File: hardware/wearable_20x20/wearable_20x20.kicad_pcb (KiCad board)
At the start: 4 copper layers, 49.3 x 49.3 mm, 400 parts

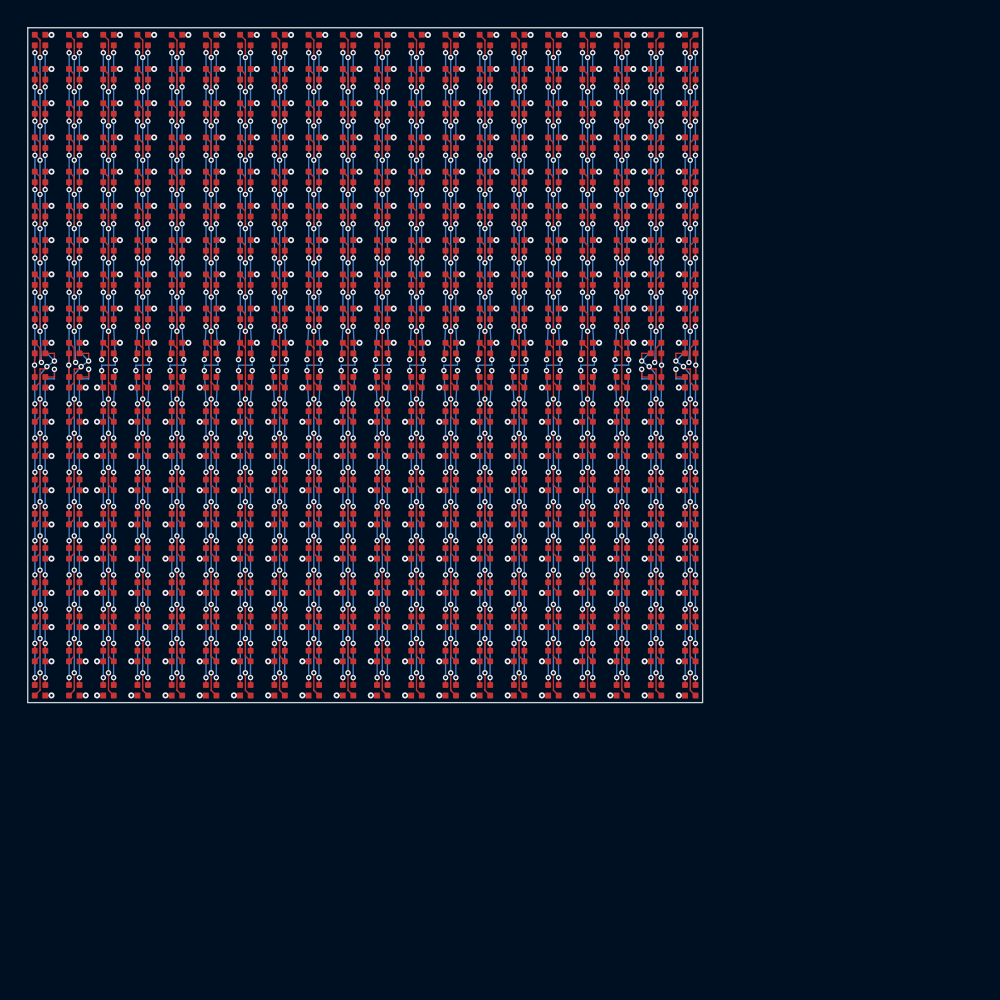
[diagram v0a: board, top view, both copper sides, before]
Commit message: Place 20x20 backside parts outside the via field
Co-authored-by: illiapliukhin <illiapliukhin@users.noreply.github.com>
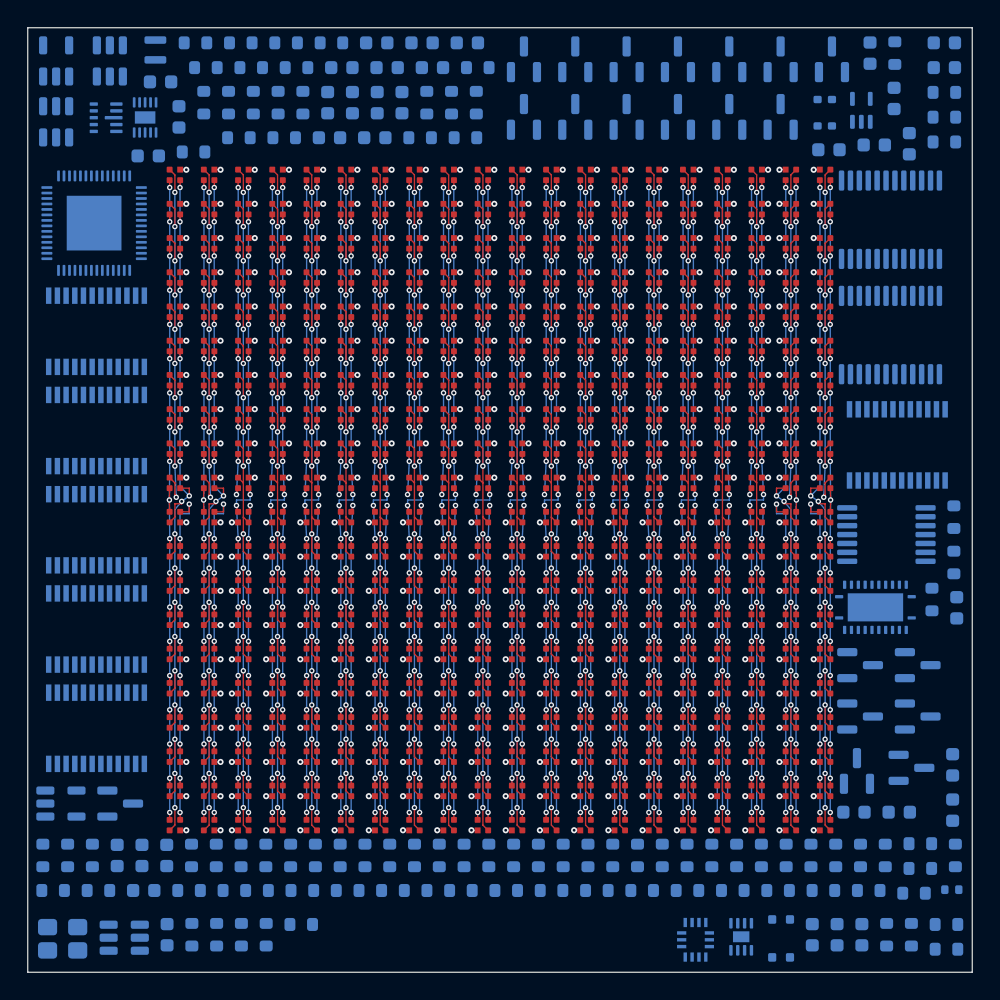
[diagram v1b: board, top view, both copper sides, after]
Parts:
- added C1: 1uF, C_0603_1608Metric, B.Cu at (22.0, 8.03)
- added C10: 10uF, C_0603_1608Metric, B.Cu at (25.5, 5.47)
- added C100: 100nF, C_0603_1608Metric, B.Cu at (67.9, 42.4)
- added C101: 100nF, C_0603_1608Metric, B.Cu at (67.6, 53.8)
- added C102: 100nF, C_0603_1608Metric, B.Cu at (67.6, 57.2)
- added C103: 100nF, C_0603_1608Metric, B.Cu at (60.4, 57.3)
- added C104: 100nF, C_0603_1608Metric, B.Cu at (63.7, 57.3)
- added C105: 100nF, C_0603_1608Metric, B.Cu at (8.80, 9.37)
- added C106: 100nF, C_0603_1608Metric, B.Cu at (9.71, 3.95)
- added C107: 100nF, C_0603_1608Metric, B.Cu at (11.1, 6.51)
- added C11: 1nF, C_0603_1608Metric, B.Cu at (27.3, 5.47)
- added C12: 10uF, C_0603_1608Metric, B.Cu at (29.6, 2.91)
- added C2: 10uF, C_0603_1608Metric, B.Cu at (21.9, 5.47)
- added C20: 1uF, C_0603_1608Metric, B.Cu at (10.2, 66.3)
- added C201: 100nF, C_0603_1608Metric, B.Cu at (6.53, 60.5)
- added C202: 100nF, C_0603_1608Metric, B.Cu at (8.47, 63.0)
- added C203: 100nF, C_0603_1608Metric, B.Cu at (8.34, 60.5)
- added C204: 100nF, C_0603_1608Metric, B.Cu at (10.2, 60.5)
- added C3: 1uF, C_0603_1608Metric, B.Cu at (22.9, 2.91)
- added C30: 100nF, C_0603_1608Metric, B.Cu at (57.3, 66.3)
- added C31: 2.2uF, C_0603_1608Metric, B.Cu at (59.1, 66.3)
- added C32: 100nF, C_0603_1608Metric, B.Cu at (60.9, 66.3)
- added C4: 1uF, C_0603_1608Metric, B.Cu at (25.5, 1.10)
- added C40: 1uF, C_0603_1608Metric, B.Cu at (58.5, 8.91)
- added C41: 100nF, C_0603_1608Metric, B.Cu at (61.8, 8.56)
- added C42: 1uF, C_0603_1608Metric, B.Cu at (61.5, 1.85)
- added C43: 100nF, C_0603_1608Metric, B.Cu at (63.3, 5.16)
- added C44: 100pF, C_0603_1608Metric, B.Cu at (64.4, 8.47)
- added C45: 22nF, C_0603_1608Metric, B.Cu at (67.0, 1.10)
- added C46: 100nF, C_0603_1608Metric, B.Cu at (67.0, 2.91)
- added C5: 4.7uF, C_0603_1608Metric, B.Cu at (23.7, 5.47)
- added C6: 10uF, C_0603_1608Metric, B.Cu at (26.3, 2.91)
- added C7: 22uF, C_0603_1608Metric, B.Cu at (28.8, 1.10)
- added C8: 22uF, C_0603_1608Metric, B.Cu at (32.1, 1.10)
- added C9: 1nF, C_0603_1608Metric, B.Cu at (25.4, 8.03)
- added L1: DFE201612E-R47M=P2 0.47uH, Murata_DFE201612E_2.0x1.6mm, B.Cu at (9.32, 1.62)
- added MIC1: NA-FFA381-A10-1, Gettop_NA-FFA381-A10-1_TopPort_Microphone, B.Cu at (58.2, 6.21)
- added Q201: AO3403, SOT-23, B.Cu at (60.8, 46.6)
- added Q202: AO3403, SOT-23, B.Cu at (65.0, 46.6)
- added Q203: AO3403, SOT-23, B.Cu at (60.8, 50.3)
- added Q204: AO3403, SOT-23, B.Cu at (65.0, 50.3)
- added Q205: AO3403, SOT-23, B.Cu at (60.6, 54.3)
- added Q206: AO3403, SOT-23, B.Cu at (64.6, 54.1)
- added Q207: AO3403, SOT-23, B.Cu at (6.75, 56.7)
- added Q208: AO3403, SOT-23, B.Cu at (36.2, 2.31)
- added Q209: AO3403, SOT-23, B.Cu at (36.2, 6.51)
- added Q210: AO3403, SOT-23, B.Cu at (40.0, 2.31)
- added Q211: AO3403, SOT-23, B.Cu at (40.0, 6.51)
- added Q212: AO3403, SOT-23, B.Cu at (43.8, 2.31)
- added Q213: AO3403, SOT-23, B.Cu at (43.8, 6.51)
- added Q214: AO3403, SOT-23, B.Cu at (47.5, 2.31)
- added Q215: AO3403, SOT-23, B.Cu at (47.5, 6.51)
- added Q216: AO3403, SOT-23, B.Cu at (51.2, 2.31)
- added Q217: AO3403, SOT-23, B.Cu at (51.2, 6.51)
- added Q218: AO3403, SOT-23, B.Cu at (55.0, 2.31)
- added Q219: AO3403, SOT-23, B.Cu at (55.0, 6.51)
- added Q220: AO3403, SOT-23, B.Cu at (58.8, 2.31)
- added R1: 24k, R_0603_1608Metric, B.Cu at (32.9, 2.91)
- added R10: 100k, R_0603_1608Metric, B.Cu at (5.16, 63.0)
- added R101: 1.96k 0.1%, R_0603_1608Metric, B.Cu at (12.1, 9.07)
- added R102: 1.96k 0.1%, R_0603_1608Metric, B.Cu at (12.3, 1.10)
- added R103: 1.96k 0.1%, R_0603_1608Metric, B.Cu at (13.0, 2.91)
- added R104: 1.96k 0.1%, R_0603_1608Metric, B.Cu at (15.6, 1.10)
- added R105: 1.96k 0.1%, R_0603_1608Metric, B.Cu at (12.9, 5.47)
- added R106: 1.96k 0.1%, R_0603_1608Metric, B.Cu at (14.7, 5.47)
- added R107: 100k, R_0603_1608Metric, B.Cu at (16.3, 2.91)
- added R108: 100k, R_0603_1608Metric, B.Cu at (18.9, 1.10)
- added R109: 100k, R_0603_1608Metric, B.Cu at (15.4, 8.03)
- added R11: DNP, R_0603_1608Metric, B.Cu at (4.72, 60.5)
- added R110: 100k, R_0603_1608Metric, B.Cu at (16.5, 5.47)
- added R111: 47k, R_0603_1608Metric, B.Cu at (18.7, 8.03)
- added R112: 47k, R_0603_1608Metric, B.Cu at (18.3, 5.47)
- added R113: 22R, R_0603_1608Metric, B.Cu at (19.6, 2.91)
- added R114: 22R, R_0603_1608Metric, B.Cu at (22.2, 1.10)
- added R115: 22R, R_0603_1608Metric, B.Cu at (20.1, 5.47)
- added R2: 1k, R_0603_1608Metric, B.Cu at (28.7, 8.03)
- added R20: 10k, R_0603_1608Metric, B.Cu at (12.0, 66.3)
- added R201: 33R, R_0603_1608Metric, B.Cu at (11.8, 63.0)
- added R202: 33R, R_0603_1608Metric, B.Cu at (12.0, 60.5)
- added R203: 33R, R_0603_1608Metric, B.Cu at (13.8, 60.5)
- added R204: 33R, R_0603_1608Metric, B.Cu at (15.1, 63.0)
- added R205: 33R, R_0603_1608Metric, B.Cu at (15.6, 60.5)
- added R206: 33R, R_0603_1608Metric, B.Cu at (17.4, 60.5)
- added R207: 33R, R_0603_1608Metric, B.Cu at (18.4, 63.0)
- added R208: 33R, R_0603_1608Metric, B.Cu at (19.2, 60.5)
- added R209: 33R, R_0603_1608Metric, B.Cu at (21.7, 63.0)
- added R21: 22R, R_0603_1608Metric, B.Cu at (13.8, 66.3)
- added R210: 33R, R_0603_1608Metric, B.Cu at (21.0, 60.5)
- added R211: 33R, R_0603_1608Metric, B.Cu at (22.8, 60.5)
- added R212: 33R, R_0603_1608Metric, B.Cu at (25.0, 63.0)
- added R213: 33R, R_0603_1608Metric, B.Cu at (24.6, 60.5)
- added R214: 33R, R_0603_1608Metric, B.Cu at (26.4, 60.5)
- added R215: 33R, R_0603_1608Metric, B.Cu at (28.3, 63.0)
- added R216: 33R, R_0603_1608Metric, B.Cu at (28.3, 60.5)
- added R217: 33R, R_0603_1608Metric, B.Cu at (30.1, 60.5)
- added R218: 33R, R_0603_1608Metric, B.Cu at (31.6, 63.0)
- added R219: 33R, R_0603_1608Metric, B.Cu at (31.9, 60.5)
- added R22: 22R, R_0603_1608Metric, B.Cu at (15.6, 66.3)
- added R220: 33R, R_0603_1608Metric, B.Cu at (33.7, 60.5)
- added R23: 5.1k, R_0603_1608Metric, B.Cu at (17.4, 66.3)
- added R24: 5.1k, R_0603_1608Metric, B.Cu at (20.0, 65.5)
- added R3: 655k 0.1%, R_0603_1608Metric, B.Cu at (29.1, 5.47)
- added R30: 4.7k, R_0603_1608Metric, B.Cu at (62.7, 66.3)
- added R301: 47k, R_0603_1608Metric, B.Cu at (35.0, 63.0)
- added R302: 47k, R_0603_1608Metric, B.Cu at (35.5, 60.5)
- added R303: 47k, R_0603_1608Metric, B.Cu at (37.3, 60.5)
- added R304: 47k, R_0603_1608Metric, B.Cu at (38.3, 63.0)
- added R305: 47k, R_0603_1608Metric, B.Cu at (39.1, 60.5)
- added R306: 47k, R_0603_1608Metric, B.Cu at (41.6, 63.0)
- added R307: 47k, R_0603_1608Metric, B.Cu at (40.9, 60.5)
- added R308: 47k, R_0603_1608Metric, B.Cu at (42.7, 60.5)
- added R309: 47k, R_0603_1608Metric, B.Cu at (44.9, 63.0)
- added R31: 4.7k, R_0603_1608Metric, B.Cu at (64.6, 66.3)
- added R310: 47k, R_0603_1608Metric, B.Cu at (44.5, 60.5)
- added R311: 47k, R_0603_1608Metric, B.Cu at (46.4, 60.5)
- added R312: 47k, R_0603_1608Metric, B.Cu at (48.2, 63.0)
- added R313: 47k, R_0603_1608Metric, B.Cu at (48.2, 60.5)
- added R314: 47k, R_0603_1608Metric, B.Cu at (50.0, 60.5)
- added R315: 47k, R_0603_1608Metric, B.Cu at (51.5, 63.0)
- added R316: 47k, R_0603_1608Metric, B.Cu at (51.8, 60.5)
- added R317: 47k, R_0603_1608Metric, B.Cu at (53.6, 60.5)
- added R318: 47k, R_0603_1608Metric, B.Cu at (54.8, 63.0)
- added R319: 47k, R_0603_1608Metric, B.Cu at (55.4, 60.5)
- added R32: 100k, R_0603_1608Metric, B.Cu at (67.1, 65.5)
- added R320: 47k, R_0603_1608Metric, B.Cu at (57.2, 60.5)
- added R33: 10k, R_0603_1608Metric, B.Cu at (67.1, 67.3)
- added R34: 0R, R_0603_1608Metric, B.Cu at (1.10, 60.5)
- added R35: 0R, R_0603_1608Metric, B.Cu at (1.85, 63.0)
- added R4: 91k 0.1%, R_0603_1608Metric, B.Cu at (31.0, 5.47)
- added R40: 100R, R_0603_1608Metric, B.Cu at (67.0, 4.72)
- added R401: 10k, R_0603_1608Metric, B.Cu at (58.1, 63.0)
- added R402: 100k, R_0603_1608Metric, B.Cu at (59.0, 60.5)
- added R403: 100k, R_0603_1608Metric, B.Cu at (61.4, 63.0)
- added R404: 100k, R_0603_1608Metric, B.Cu at (60.8, 60.5)
- added R405: 100k, R_0603_1608Metric, B.Cu at (62.6, 60.5)
- added R406: 47k, R_0603_1608Metric, B.Cu at (65.2, 59.6)
- added R407: 47k, R_0603_1608Metric, B.Cu at (67.8, 60.5)
- added R408: 0R, R_0603_1608Metric, B.Cu at (65.2, 61.4)
- added R409: 0R, R_0603_1608Metric, B.Cu at (64.7, 63.2)
- added R41: 47k, R_0603_1608Metric, B.Cu at (67.0, 6.53)
- added R42: 47k, R_0603_1608Metric, B.Cu at (67.0, 8.34)
- added R43: 10k, R_0603_1608Metric, B.Cu at (63.3, 1.85)
- added R44: 200k, R_0603_1608Metric, B.Cu at (67.7, 35.8)
- added R45: 1k, R_0603_1608Metric, B.Cu at (67.7, 39.1)
- added R46: 100k, R_0603_1608Metric, B.Cu at (66.1, 41.8)
- added R5: 100k, R_0603_1608Metric, B.Cu at (32.8, 5.47)
- added R6: 100k, R_0603_1608Metric, B.Cu at (32.0, 8.03)
- added R7: 1k, R_0603_1608Metric, B.Cu at (2.91, 60.5)
- added SW1: EVPBL2A1F000, Panasonic_EVPBL2A1F000_Switch, B.Cu at (55.0, 66.5)
- added TH1: TE 20021086-05 10k 1% B3435, R_0402_1005Metric, B.Cu at (67.5, 63.0)
- added U1: BQ25185, Texas_DLH0010A_WSON-10-1EP_2.2x2mm_P0.4mm_EP0.9x1.5mm, B.Cu at (8.57, 6.55)
- added U10: ESP32-S3FN8, QFN-56-1EP_7x7mm_P0.4mm_EP4x4mm, B.Cu at (4.85, 14.3)
- added U100: SN74LV125APWR, TSSOP-14_4.4x5mm_P0.65mm, B.Cu at (62.7, 37.0)
- added U101: MBI5124GP-B, SSOP-24_3.9x8.7mm_P0.635mm, B.Cu at (5.03, 22.2)
- added U102: MBI5124GP-B, SSOP-24_3.9x8.7mm_P0.635mm, B.Cu at (5.03, 29.4)
- added U103: MBI5124GP-B, SSOP-24_3.9x8.7mm_P0.635mm, B.Cu at (5.03, 36.7)
- added U104: MBI5124GP-B, SSOP-24_3.9x8.7mm_P0.635mm, B.Cu at (5.03, 43.9)
- added U105: MBI5124GP-B, SSOP-24_3.9x8.7mm_P0.635mm, B.Cu at (5.03, 51.2)
- added U106: MBI5124GP-B, SSOP-24_3.9x8.7mm_P0.635mm, B.Cu at (63.5, 30.5)
- added U107: SN74LVC1G125DBVR, SOT-23-5, B.Cu at (2.42, 56.7)
- added U11: USBLC6-2SC6, SOT-23-6, B.Cu at (7.05, 66.5)
- added U2: TPS7A2033PDBVR, SOT-23-5, B.Cu at (2.08, 2.42)
- added U20: BMI270, Bosch_LGA-14_3x2.5mm_P0.5mm, B.Cu at (48.8, 66.6)
- added U201: SN74LVC8T245RHLR, TI_RHL0024A_VQFN-24-1EP_3.5x5.5mm_P0.5mm_EP2.05x4.05mm, B.Cu at (61.9, 42.3)
- added U202: 74HC154PW,118, TSSOP-24_4.4x7.8mm_P0.65mm, B.Cu at (63.0, 14.0)
- added U203: 74HC154PW,118, TSSOP-24_4.4x7.8mm_P0.65mm, B.Cu at (63.0, 22.4)
- added U21: MAX17048G+T10, TDFN-8-1EP_2x2mm_P0.5mm_EP0.8x1.2mm, B.Cu at (52.1, 66.4)
- added U3: TPS63802DLAR, TI_DLA0010A_VSON-HR-10_2x3mm_P0.5mm, B.Cu at (5.72, 6.58)
- added U30: TLV9001IDCKR, SOT-353_SC-70-5, B.Cu at (60.9, 6.04)
- added U4: TPS22917DBVR, SOT-23-6, B.Cu at (2.08, 6.88)
- added U5: TPS22917DBVR, SOT-23-6, B.Cu at (6.00, 2.42)
- added Y1: L327S400H11L 40MHz 10pF, Lucki_L327S400H11L_Crystal_3225-4Pin, B.Cu at (2.55, 66.6)
- moved D1 13.9 mm to (10.8, 10.8)
- moved D101 13.9 mm to (10.8, 23.2)
- moved D104 13.9 mm to (18.2, 23.2)
- moved D105 13.9 mm to (20.8, 23.2)
- moved D106 13.9 mm to (23.2, 23.2)
- moved D107 13.9 mm to (25.8, 23.2)
- moved D121 13.9 mm to (10.8, 25.8)
- moved D124 13.9 mm to (18.2, 25.8)
- moved D125 13.9 mm to (20.8, 25.8)
- moved D126 13.9 mm to (23.2, 25.8)
- moved D127 13.9 mm to (25.8, 25.8)
- moved D4 13.9 mm to (18.2, 10.8)
- moved D5 13.9 mm to (20.8, 10.8)
- moved D6 13.9 mm to (23.2, 10.8)
- moved D61 13.9 mm to (10.8, 18.2)
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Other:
- board size 49.3 x 49.3 mm -> 69 x 69 mm

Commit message: Route the first 20x20 column and anode escapes.
The border router stays on B.Cu and In2.Cu, leaves L2 empty, and connects 19 of 80 column/anode pads with zero DRC violations. The remaining driver pins are blocked by the 90-degree package gap, which fits one track.

Co-authored-by: illiapliukhin <illiapliukhin@users.noreply.github.com>
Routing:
- net ROW_02_ANODE: track 62.5 -> 156.2 mm, vias 20 -> 23
- net ROW_19_ANODE: track 62.5 -> 122.2 mm, vias 20 -> 21
- net ROW_17_ANODE: track 62.5 -> 120.5 mm, vias 20 -> 21
- net ROW_15_ANODE: track 62.5 -> 118.7 mm, vias 20 -> 21
- net ROW_13_ANODE: track 62.5 -> 117.0 mm, vias 20 -> 21
- net ROW_11_ANODE: track 54.8 -> 108.1 mm, vias 20 -> 21
- net COL_G_09: track 57.3 -> 109.7 mm, vias 20 -> 21
- net ROW_09_ANODE: track 62.5 -> 112.6 mm, vias 20 -> 21
- net ROW_01_ANODE: track 54.8 -> 102.9 mm, vias 20 -> 21
- net COL_G_08: track 57.3 -> 103.0 mm
- net COL_R_08: track 57.3 -> 100.0 mm, vias 20 -> 21
- net COL_B_09: track 78.8 -> 119.8 mm, vias 18 -> 19
- net COL_B_17: track 78.8 -> 118.2 mm, vias 18 -> 19
- net COL_R_09: track 57.3 -> 95.4 mm
- net COL_B_18: track 78.8 -> 114.9 mm, vias 18 -> 19
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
